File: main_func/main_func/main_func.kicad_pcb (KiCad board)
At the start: 2 copper layers, 170 x 85 mm, 121 parts, among them IC1 LN4056-ESOP8, J1 USB_C_Receptacle_USB2.0, J2 Conn_01x04_Male, J3 Battery, TEMP, J4 Korean Hroparts Elec PJ-3250-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, J8 Conn_01x02_Male, J9 Conn_01x06_Male, M3 MountingHole_3.2mm_M3, Q1 CJ2301, SW1 SW_DPDT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

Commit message: Pot.but_pcb in progress
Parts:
- J8: footprint Connector_PinSocket_2.54mm:PinSocket_1x02_P2.54mm_Horizontal -> Capacitor_THT:C_Rect_L7.5mm_W6.5mm_P5.00mm
- moved J8 5.26 mm to (207.8, 51.1), turned to 180 degrees
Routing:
- net GND: track 260.0 -> 268.8 mm, vias 866 -> 825
- net SOUTL: track 13.3 -> 15.9 mm
- net SOUTR: track 10.1 -> 7.95 mm
- net (no net): vias 3 -> 0

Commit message: pcb design fixing
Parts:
- removed J8: Conn_01x02_Male, Capacitor_THT:C_Rect_L7.5mm_W6.5mm_P5.00mm
- removed the M3 at (214.5, 50.5)
- removed the M3 at (214.5, 124.5)
- removed the M3 at (55.5, 124.5)
- removed the M3 at (55.5, 50.5)
- removed TP1, TP2: TestPoint, TestPoint:TestPoint_Keystone_5010-5014_Multipurpose
- added J5: Battery, TEMP, Connector_PinHeader_2.54mm:PinHeader_1x04_P2.54mm_Horizontal, F.Cu at (73.0, 94.5)
- added J6: Conn_01x04_Male, Connector_PinHeader_2.54mm:PinHeader_1x04_P2.54mm_Vertical, F.Cu at (184.4, 63.7)
- added M3: MountingHole_3.2mm_M3, MountingHole:MountingHole_3.2mm_M3, F.Cu at (213.0, 123.5)
- added M3: MountingHole_3.2mm_M3, MountingHole:MountingHole_3.2mm_M3, F.Cu at (55.0, 49.5)
- added M3: MountingHole_3.2mm_M3, MountingHole:MountingHole_3.2mm_M3, F.Cu at (55.0, 123.5)
- added M3: MountingHole_3.2mm_M3, MountingHole:MountingHole_3.2mm_M3, F.Cu at (175.5, 50.0)
- C13, C9: value 10u -> 100n
- J2: value Conn_01x04_Male -> Conn_01x10_Male; footprint Connector_PinHeader_2.54mm:PinHeader_1x04_P2.54mm_Horizontal -> Connector_IDC:IDC-Header_2x05_P2.54mm_Horizontal
- J3: value Battery, TEMP -> Conn_01x10_Male; footprint Connector_PinSocket_2.54mm:PinSocket_1x03_P2.54mm_Horizontal -> Connector_IDC:IDC-Header_2x05_P2.54mm_Horizontal
- R40: value 100k -> 10k
- moved U8 56.5 mm to (122.0, 63.0), turned to 0 degrees
- moved U9 55.3 mm to (161.0, 63.0), turned to 0 degrees
- moved R5 54.6 mm to (173.3, 112.5)
- moved R6 54.5 mm to (173.4, 108.8)
- moved U4 51.1 mm to (187.1, 107.0), turned to 180 degrees
- moved R7 50.6 mm to (173.5, 105.1)
- moved C6 48.1 mm to (199.2, 124.3), turned to 0 degrees
- moved D4 47.5 mm to (161.7, 69.4), turned to 180 degrees
- moved C16 46.7 mm to (166.2, 84.5), turned to 0 degrees
- moved R23 44.4 mm to (121.7, 68.2), turned to 180 degrees
- moved C8 43.7 mm to (199.2, 120.5), turned to 0 degrees
- moved L1 43.0 mm to (192.7, 123.6), turned to 90 degrees
- moved R12 42.2 mm to (173.3, 98.0)
- moved C13 40.4 mm to (204.2, 108.0), turned to 0 degrees
- moved C7 40.0 mm to (199.2, 117.2), turned to 0 degrees
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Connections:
- net VERF renamed VREF
- J2 pad 1: I2C1_SDA -> LOAD
- J2 pad 2: I2C1_SCL -> GND
- J3 pad 1: VBATT -> LOAD
- J3 pad 3: /Power_dcdc/Battery_chargerm/TEMP -> LOAD
- U4 pad 11: Net-(TP1-Pad1) -> unconnected-(U4-Pad11)
- U4 pad 12: Net-(TP2-Pad1) -> unconnected-(U4-Pad12)
- U4 pad 6: 5V_VCCda -> 5VA
- U7 pad 14: WKUPm -> unconnected-(U7-Pad14)
- U9 pad 2: GND -> MIDI_IN_GND
- U9 pad 6: GND -> MIDI_IN_GND
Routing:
- net GND: track 268.8 -> 132.5 mm, vias 825 -> 1082
- net VREF: track 125.2 -> 24.6 mm, vias 0 -> 2
- net VOUTLda: track 88.4 -> 16.7 mm, vias 2 -> 0
- net DATAda: track 22.3 -> 81.6 mm, vias 0 -> 2
- net BCLKda: track 24.5 -> 81.8 mm, vias 0 -> 2
- net VOUTRda: track 62.3 -> 5.02 mm, vias 2 -> 0
- net I2S1_WSm: track 27.1 -> 78.2 mm
- net I2C1_SCL: track 41.3 -> 88.4 mm, vias 0 -> 3
- net I2C1_SDA: track 39.8 -> 85.3 mm, vias 0 -> 3
- net MLda: track 46.3 -> 91.6 mm
- net 5VA: track 105.0 -> 61.6 mm, vias 5 -> 2
- net MCda: track 40.5 -> 79.1 mm, vias 0 -> 2
- net I2S1_MCKm: track 44.6 -> 79.5 mm
- net MDda: track 50.1 -> 76.6 mm, vias 0 -> 2
- net LOAD: track 184.0 -> 208.7 mm, vias 3 -> 5
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- added copper zone on B.Cu, net MIDI_IN_GND
- added copper zone on F.Cu, net MIDI_IN_GND

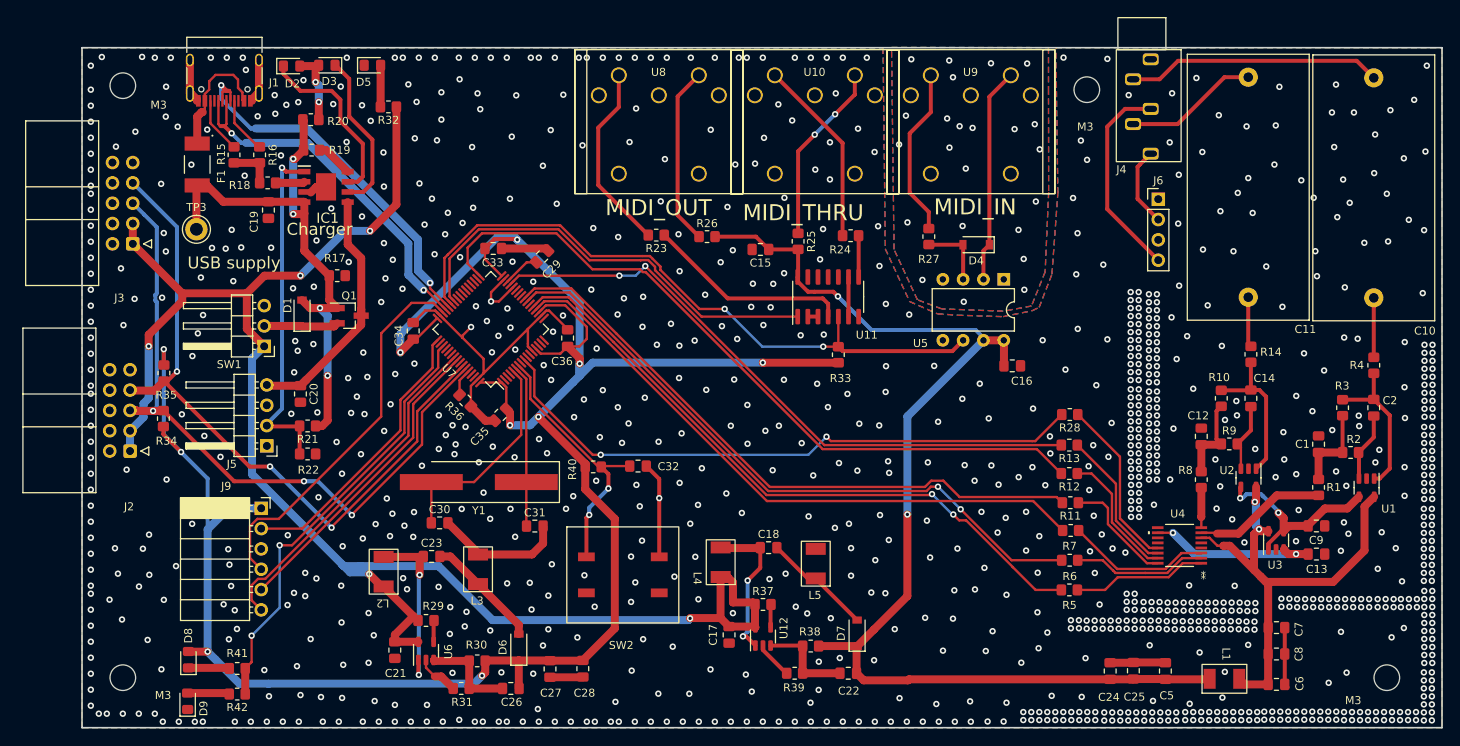
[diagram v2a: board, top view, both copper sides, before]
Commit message: pcb mounting hole change
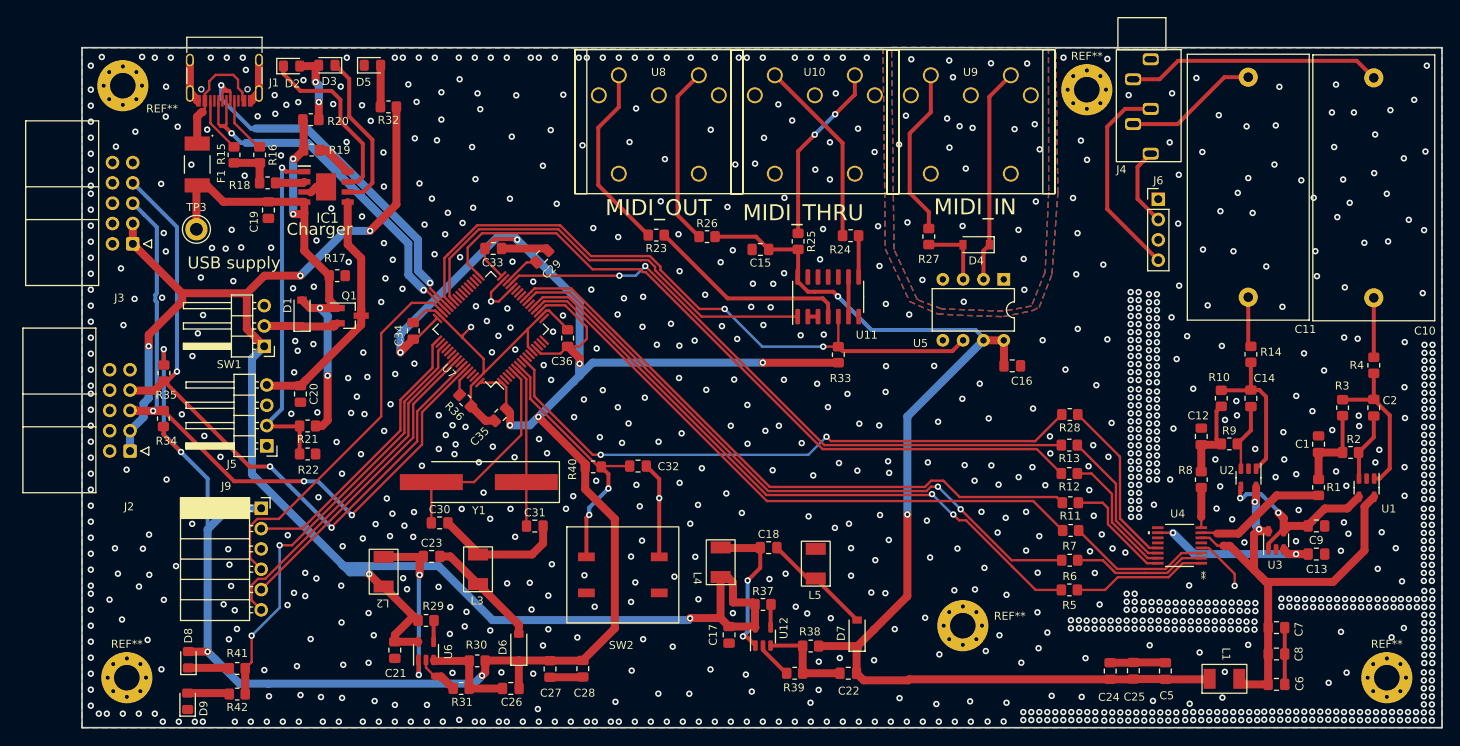
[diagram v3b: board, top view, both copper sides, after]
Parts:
- removed M3 (x4): MountingHole_3.2mm_M3, MountingHole:MountingHole_3.2mm_M3
- added REF**: MountingHole_3.2mm_M3_Pad_Via, MountingHole:MountingHole_3.2mm_M3_Pad_Via, F.Cu at (160.0, 117.0)
- added REF**: MountingHole_3.2mm_M3_Pad_Via, MountingHole:MountingHole_3.2mm_M3_Pad_Via, F.Cu at (55.5, 123.5)
- added REF**: MountingHole_3.2mm_M3_Pad_Via, MountingHole:MountingHole_3.2mm_M3_Pad_Via, F.Cu at (55.0, 49.5)
- added REF**: MountingHole_3.2mm_M3_Pad_Via, MountingHole:MountingHole_3.2mm_M3_Pad_Via, F.Cu at (175.5, 50.0)
- added REF**: MountingHole_3.2mm_M3_Pad_Via, MountingHole:MountingHole_3.2mm_M3_Pad_Via, F.Cu at (213.0, 123.5)
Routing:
- net GND: track 132.5 -> 139.5 mm, vias 1082 -> 1081

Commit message: gerber files generated
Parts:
- removed REF** (x5): MountingHole_3.2mm_M3_Pad_Via, MountingHole:MountingHole_3.2mm_M3_Pad_Via
- added H1: MountingHole, MountingHole:MountingHole_3.2mm_M3_Pad_Via, F.Cu at (55.0, 50.0)
- added H2: MountingHole, MountingHole:MountingHole_3.2mm_M3_Pad_Via, F.Cu at (55.0, 123.0)
- added H3: MountingHole, MountingHole:MountingHole_3.2mm_M3_Pad_Via, F.Cu at (160.0, 117.0)
- added H4: MountingHole, MountingHole:MountingHole_3.2mm_M3_Pad_Via, F.Cu at (213.0, 123.0)
- added H5: MountingHole, MountingHole:MountingHole_3.2mm_M3_Pad_Via, F.Cu at (175.5, 50.0)
- moved J3 1.35 mm to (55.1, 70.0)
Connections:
- U11 pad 11: unconnected-(U11-Pad11) -> GND
- U11 pad 13: unconnected-(U11-Pad13) -> GND
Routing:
- net LOAD: track 208.7 -> 209.6 mm
- net I2C1_SDA: track 85.3 -> 86.2 mm
- net I2C1_SCL: track 88.4 -> 89.2 mm
